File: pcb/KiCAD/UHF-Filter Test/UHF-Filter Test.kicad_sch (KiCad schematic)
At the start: 18 parts, among them J1 Antenna, J2 SMA, J3 Radio, J4 SMA

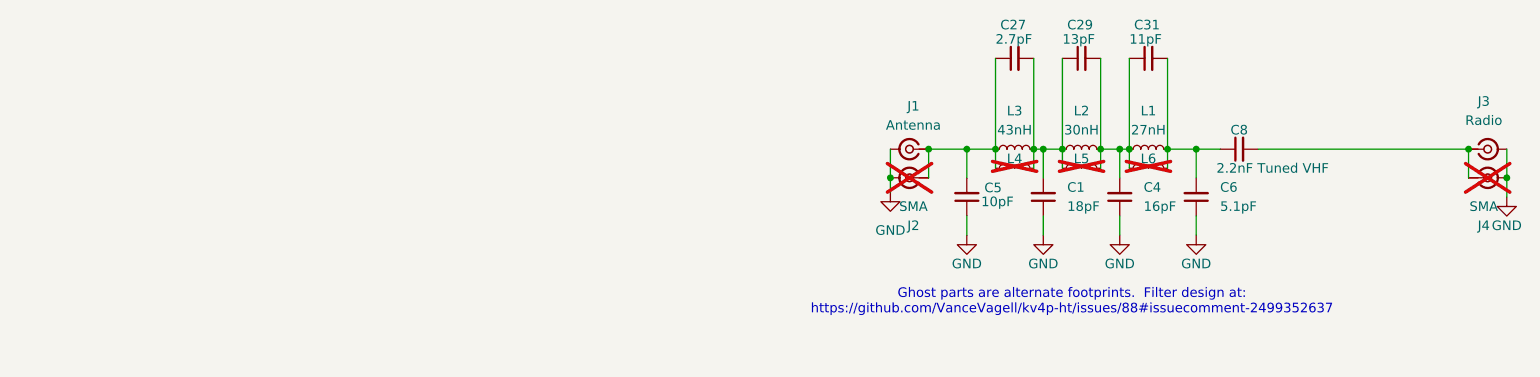
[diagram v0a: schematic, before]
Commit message: Split Filter\ Test into VHF and UHF versions. Order VHF yesterday, UHF today. #22
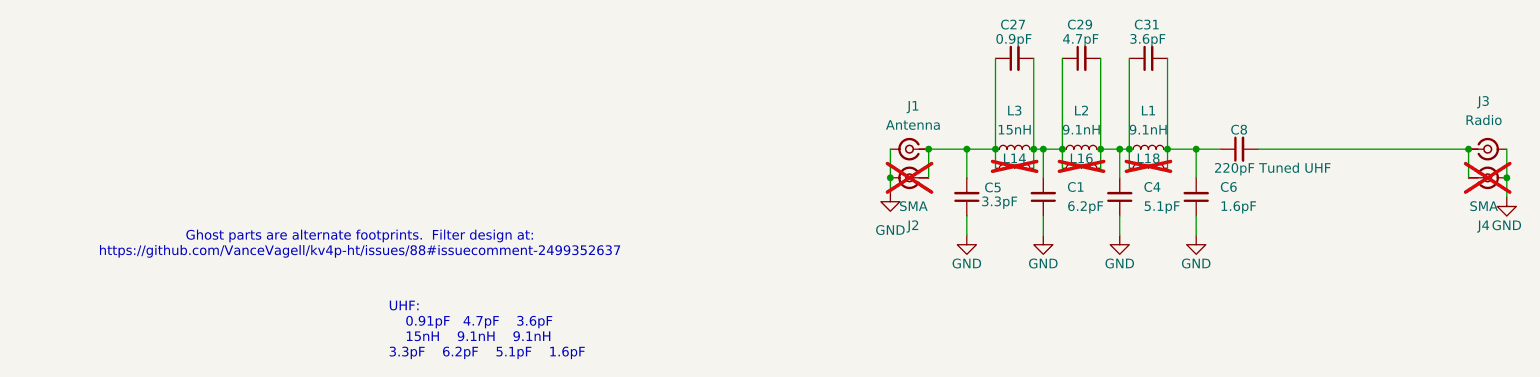
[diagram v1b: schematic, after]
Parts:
- removed L4: ~, Inductor_SMD:L_0805_2012Metric, symbol Device:L_Small
- removed L5, L6: ~, Inductor_SMD:L_0603_1608Metric, symbol Device:L_Small
- added L14: ~, Inductor_SMD:L_0603_1608Metric, symbol Device:L_Small
- added L16, L18: ~, Inductor_SMD:L_0805_2012Metric, symbol Device:L_Small
- C1: value 18pF -> 6.2pF; LCSC C1549 -> C161331; Part Number Ya basic. -> GJM1555C1H6R2BB01D
- C27: value 2.7pF -> 0.9pF; LCSC C1561 -> C161350; Part Number (none) -> GJM1555C1HR90WB01D
- C29: value 13pF -> 4.7pF; LCSC C393681 -> C161327; Part Number (none) -> GJM1555C1H4R7BB01D
- C31: value 11pF -> 3.6pF; LCSC C527000 -> C161320; Part Number (none) -> GJM1555C1H3R6BB01D
- C4: value 16pF -> 5.1pF; LCSC C77590 -> C237535; Part Number CC0402JRNPO9BN160 -> GJM1555C1H5R1BB01D
- C5: value 10pF -> 3.3pF; LCSC C32949 -> C88892; Part Number Ya so basic. -> GJM1555C1H3R3WB01D
- C6: value 5.1pF -> 1.6pF; LCSC C60220 -> C88881; Part Number (none) -> GJM1555C1H1R6WB01D
- C8: value 2.2nF Tuned VHF -> 220pF Tuned UHF; LCSC C2168957 -> C388907; Part Number GCM1885C1H222FA16D -> GCM1885C2A221JA16D
- L1: value 27nH -> 9.1nH; footprint Inductor_SMD:L_0805_2012Metric -> Inductor_SMD:L_0603_1608Metric; Alternate LCSC (none) -> C2049208 preferred; LCSC C1330812 -> C77125; Part Number LQW2BAN27NJ00L -> LQW18AN9N1G80D preferred, LQW18AN9N1D00D spec'd
- L2: value 30nH -> 9.1nH; footprint Inductor_SMD:L_0805_2012Metric -> Inductor_SMD:L_0603_1608Metric; Alternate LCSC C3221803 -> C2049208 preferred; LCSC C5137205 -> C77125; Part Number FHW0805UC030JGT -> LQW18AN9N1G80D preferred, LQW18AN9N1D00D spec'd
- L3: value 43nH -> 15nH; footprint Inductor_SMD:L_0603_1608Metric -> Inductor_SMD:L_0805_2012Metric; Alternate LCSC C1330253 (0805) -> C3222503 (preferred); LCSC C574016 -> C341794; Part Number SWI0603F-43NG -> LQW2BAN15NG00L (preferred) , LQW2BAS15NG00L spec'd
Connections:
- net at C27.1, C5.2, J1.1 (In)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: now also L14.1
- net at C1.2, C27.2, C29.1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: now also L14.2, L16.1
- net at C29.2, C31.1, C4.2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: now also L16.2, L18.1
- net at C31.2, C6.2, C8.1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: now also L18.2
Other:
- note added: "UHF: 0.91pF 4.7pF 3.6pF 15nH 9.1nH 9.1nH 3.3pF 6.2pF 5.1pF 1.6pF"
